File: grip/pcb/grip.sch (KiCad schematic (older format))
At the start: 4 parts, among them U1 MAN71A, U2 MAN71A

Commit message: grip: finished 1 layered pcb
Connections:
- net GND: no longer A1.29 (GND)
- net deci_A: now also A1.13 (D10); no longer A1.12 (D9)
- net deci_B: now also A1.12 (D9); no longer A1.13 (D10)
- net deci_C: now also A1.20 (A1); no longer A1.14 (D11)
- net deci_G: now also A1.14 (D11); no longer A1.20 (A1)
- net unit_D: now also A1.11 (D8); no longer A1.8 (D5)
- net unit_E: now also A1.10 (D7); no longer A1.9 (D6)
- net unit_F: now also A1.9 (D6); no longer A1.10 (D7)
- net unit_G: now also A1.8 (D5); no longer A1.11 (D8)
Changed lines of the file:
@@
 $EndComp
-Wire Wire Line
-	5000 6600 4900 6600
-Connection ~ 4900 6600
 Wire Wire Line
 	7850 5900 7850 6000
@@
 Text GLabel 4400 5400 0    50   Input ~ 0
 unit_C
+Text GLabel 4400 5800 0    50   Input ~ 0
+unit_D
+Text GLabel 4400 5700 0    50   Input ~ 0
+unit_E
+Text GLabel 4400 5600 0    50   Input ~ 0
+unit_F
 Text GLabel 4400 5500 0    50   Input ~ 0
-unit_D
-Text GLabel 4400 5600 0    50   Input ~ 0
-unit_E
-Text GLabel 4400 5700 0    50   Input ~ 0
-unit_F
-Text GLabel 4400 5800 0    50   Input ~ 0
 unit_G
+Text GLabel 4400 6000 0    50   Input ~ 0
+deci_A
 Text GLabel 4400 5900 0    50   Input ~ 0
-deci_A
-Text GLabel 4400 6000 0    50   Input ~ 0
 deci_B
-Text GLabel 4400 6100 0    50   Input ~ 0
+Text GLabel 5400 5700 2    50   Input ~ 0
 deci_C
 Text GLabel 4400 6200 0    50   Input ~ 0
@@
 Text GLabel 5400 5600 2    50   Input ~ 0
 deci_F
-Text GLabel 5400 5700 2    50   Input ~ 0
+Text GLabel 4400 6100 0    50   Input ~ 0
 deci_G
 Text GLabel 8800 5200 0    50   Input ~ 0

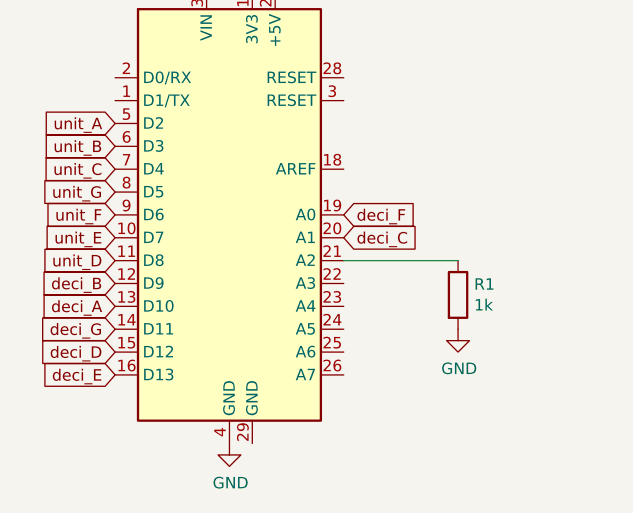
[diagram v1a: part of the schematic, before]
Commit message: grip: changed pcb for a line layout
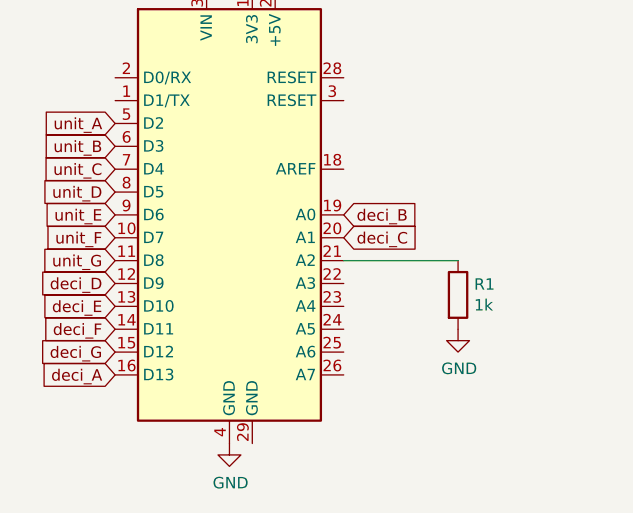
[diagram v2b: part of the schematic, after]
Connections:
- net deci_A: now also A1.16 (D13); no longer A1.13 (D10)
- net deci_B: now also A1.19 (A0); no longer A1.12 (D9)
- net deci_D: now also A1.12 (D9); no longer A1.15 (D12)
- net deci_E: now also A1.13 (D10); no longer A1.16 (D13)
- net deci_F: now also A1.14 (D11); no longer A1.19 (A0)
- net deci_G: now also A1.15 (D12); no longer A1.14 (D11)
- net unit_D: now also A1.8 (D5); no longer A1.11 (D8)
- net unit_E: now also A1.9 (D6); no longer A1.10 (D7)
- net unit_F: now also A1.10 (D7); no longer A1.9 (D6)
- net unit_G: now also A1.11 (D8); no longer A1.8 (D5)
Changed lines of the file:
@@
 Text GLabel 4400 5400 0    50   Input ~ 0
 unit_C
+Text GLabel 4400 5500 0    50   Input ~ 0
+unit_D
+Text GLabel 4400 5600 0    50   Input ~ 0
+unit_E
+Text GLabel 4400 5700 0    50   Input ~ 0
+unit_F
 Text GLabel 4400 5800 0    50   Input ~ 0
-unit_D
-Text GLabel 4400 5700 0    50   Input ~ 0
-unit_E
-Text GLabel 4400 5600 0    50   Input ~ 0
-unit_F
-Text GLabel 4400 5500 0    50   Input ~ 0
 unit_G
-Text GLabel 4400 6000 0    50   Input ~ 0
+Text GLabel 4400 6300 0    50   Input ~ 0
 deci_A
-Text GLabel 4400 5900 0    50   Input ~ 0
+Text GLabel 5400 5600 2    50   Input ~ 0
 deci_B
 Text GLabel 5400 5700 2    50   Input ~ 0
 deci_C
+Text GLabel 4400 5900 0    50   Input ~ 0
+deci_D
+Text GLabel 4400 6000 0    50   Input ~ 0
+deci_E
+Text GLabel 4400 6100 0    50   Input ~ 0
+deci_F
 Text GLabel 4400 6200 0    50   Input ~ 0
-deci_D
-Text GLabel 4400 6300 0    50   Input ~ 0
-deci_E
-Text GLabel 5400 5600 2    50   Input ~ 0
-deci_F
-Text GLabel 4400 6100 0    50   Input ~ 0
 deci_G
 Text GLabel 8800 5200 0    50   Input ~ 0

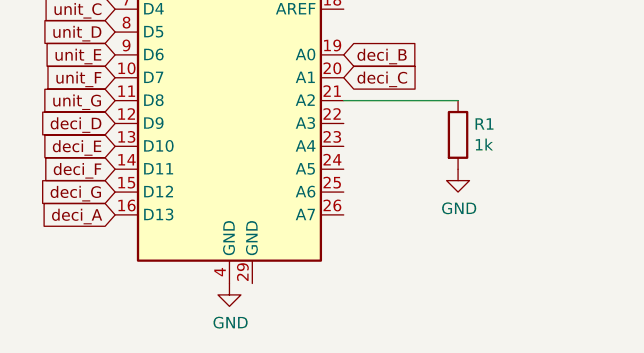
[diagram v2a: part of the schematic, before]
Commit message: correcte mutt template
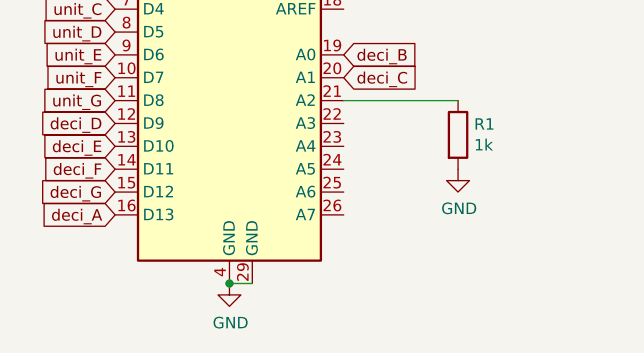
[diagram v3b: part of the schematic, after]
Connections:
- net GND: now also A1.29 (GND)
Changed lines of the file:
@@
 Wire Wire Line
 	5400 5800 5900 5800
+Wire Wire Line
+	5000 6600 4900 6600
+Connection ~ 4900 6600
 $EndSCHEMATC
